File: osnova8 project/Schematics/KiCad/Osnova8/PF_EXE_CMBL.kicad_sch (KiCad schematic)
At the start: 10 parts, among them U38 74LS08, U39 74LS08, U41 74LS00, U42 74LS00

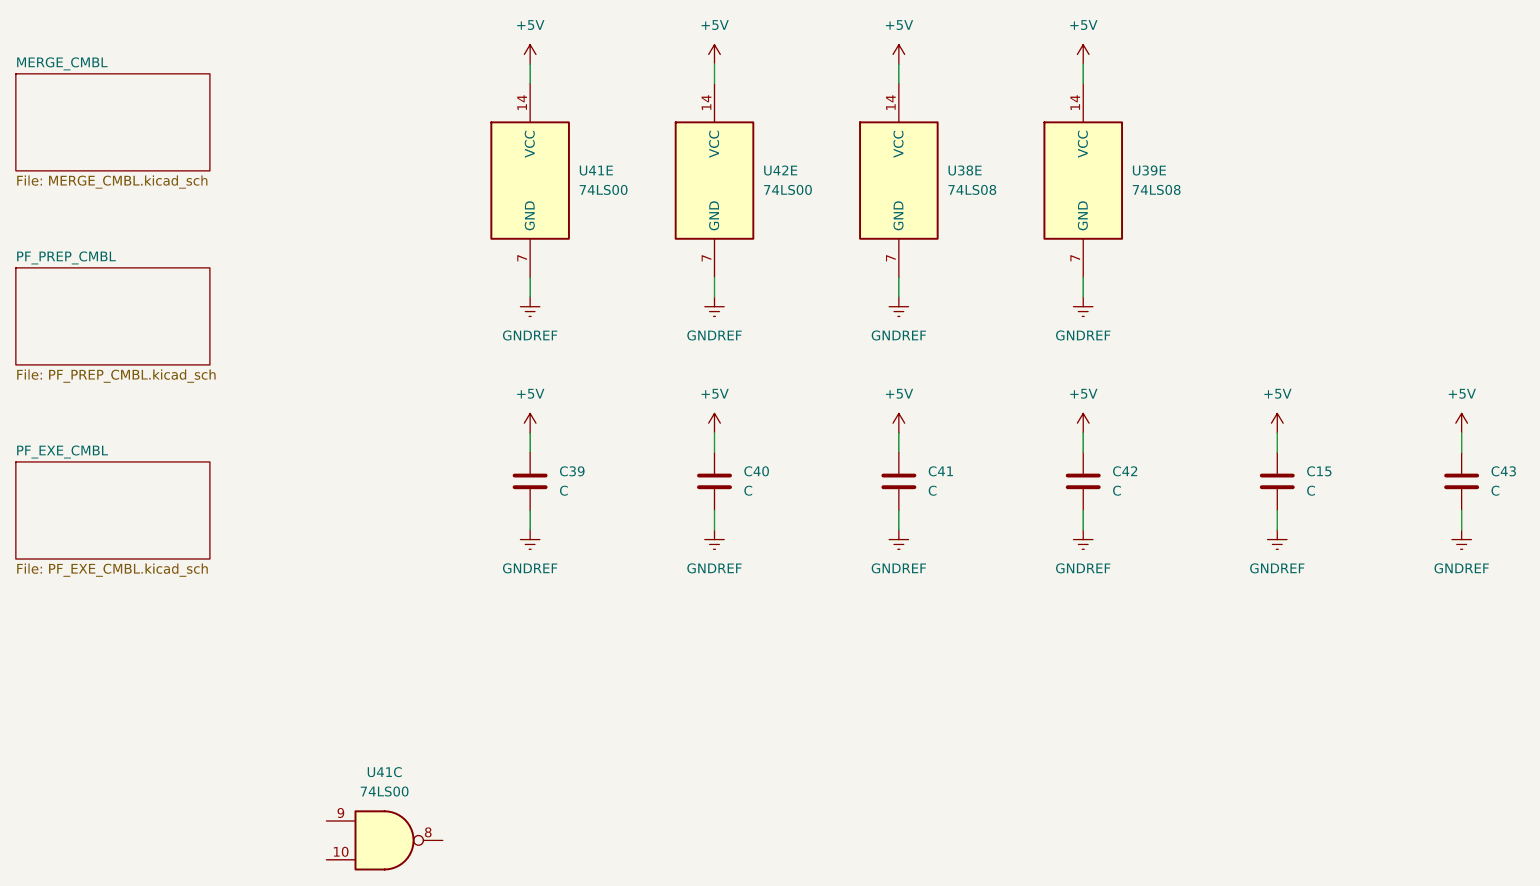
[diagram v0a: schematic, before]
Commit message: updated schematics
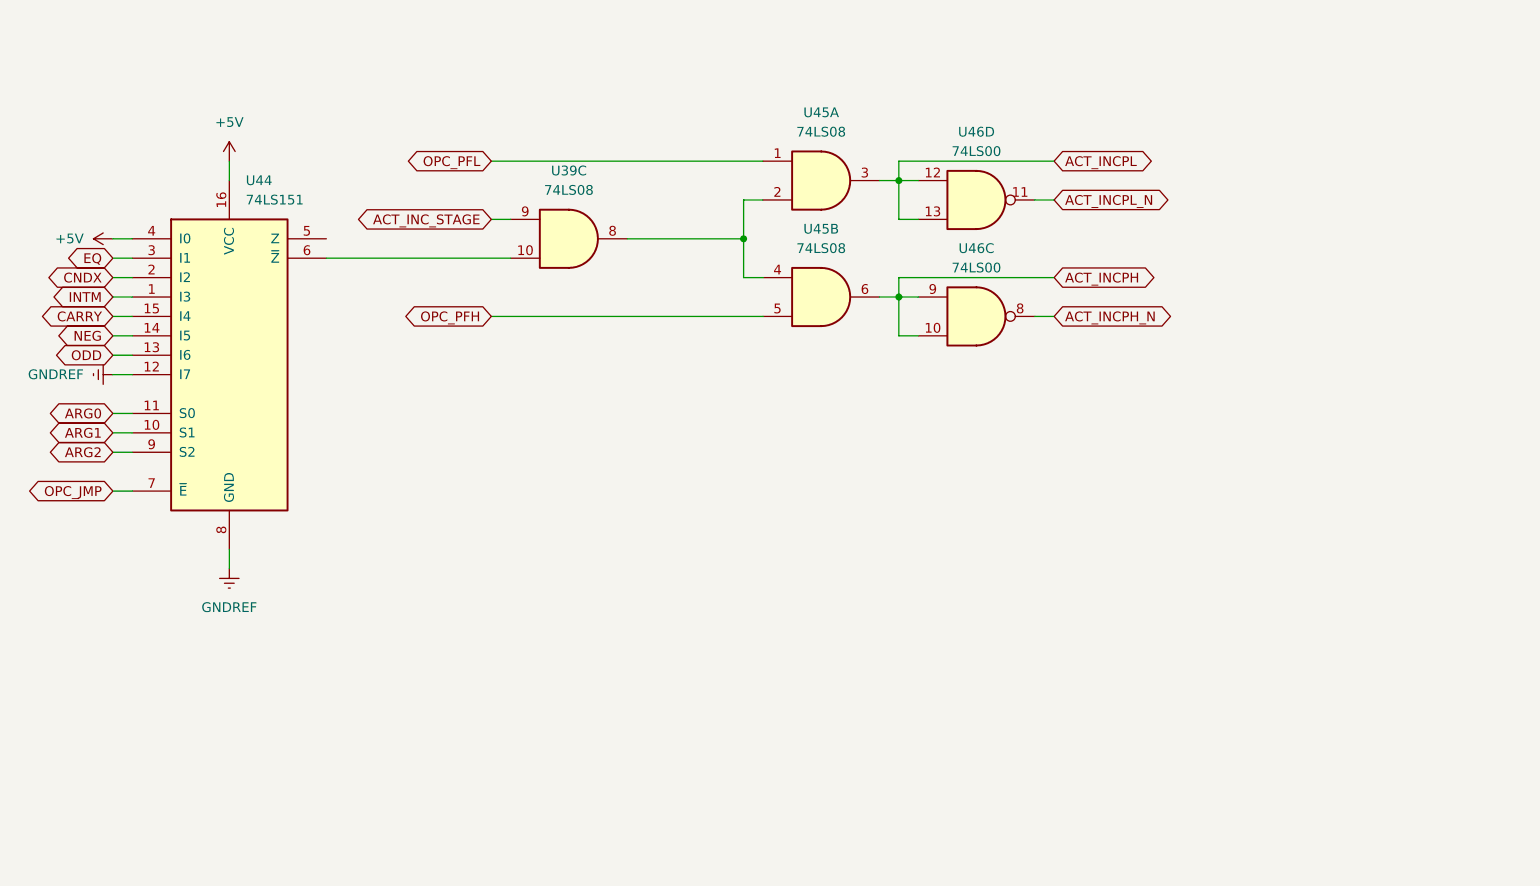
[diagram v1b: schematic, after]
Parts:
- removed C15, C39, C40, C41, C42, C43: C, symbol Device:C
- removed U38, U39: 74LS08, symbol 74xx:74LS08
- removed U41, U42: 74LS00, symbol 74xx:74LS00
- added U39, U45: 74LS08, symbol 74xx:74LS08
- added U44: 74LS151, symbol 74xx:74LS151
- added U46: 74LS00, symbol 74xx:74LS00
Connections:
- net +5V: now also U44.16 (VCC), U44.4 (I0)
- net GNDREF: now also U44.12 (I7), U44.8 (GND)
- new net: U39.10, U44.6 (~{Z})
- new net: U39.8, U45.2, U45.4
- new net ACT_INCPH: U45.6, U46.10, U46.9
- new net ACT_INCPH_N: U46.8
- new net ACT_INCPL: U45.3, U46.12, U46.13
- new net ACT_INCPL_N: U46.11
- new net ACT_INC_STAGE: U39.9
- new net ARG0: U44.11 (S0)
- new net ARG1: U44.10 (S1)
- new net ARG2: U44.9 (S2)
- new net CARRY: U44.15 (I4)
- new net CNDX: U44.2 (I2)
- new net EQ: U44.3 (I1)
- new net INTM: U44.1 (I3)
- new net NEG: U44.14 (I5)
- new net ODD: U44.13 (I6)
- new net OPC_JMP: U44.7 (~{E})
- new net OPC_PFH: U45.5
- new net OPC_PFL: U45.1
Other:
- removed sheet MERGE_CMBL
- removed sheet PF_EXE_CMBL
- removed sheet PF_PREP_CMBL
